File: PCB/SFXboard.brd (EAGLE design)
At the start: 34 x 31.7 mm, 17 parts, among them J1 AVR_SPI_PRG_62X3_LOCK, J2 TERMBLOCK4POS, J3 POWER_JACKPTH, Q1 16MHz, Q2 BSS138, Q3 BSS138, Q4 BSS138, U1 ATMEGA16U2-AU, X1 USBSMD

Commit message: Begin working on better power filtering, misc enhancements
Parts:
- added C5: 22uF, resistor:C0805
- added SJ1: (no value), jumper:SJ
- J1: value AVR_SPI_PRG_62X3_LOCK -> AVR_SPI_PRG_6PTH; device SparkFun-Connectors:2X3_LOCK -> SparkFun-Connectors:2X3
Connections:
- new net N$17: SJ1.1, U1.13
- net GND: now also C5.2, SJ1.2
- net N$16: now also C5.1
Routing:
- net N$16: track 26.4 -> 27.4 mm
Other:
- board text added: "Rev 2012-10-14.1"
- board text removed: "Rev 2012-09-16.1"
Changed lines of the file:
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@@
 <layer number="19" name="Unrouted" color="6" fill="1" visible="yes" active="yes"/>
 <layer number="20" name="Dimension" color="15" fill="1" visible="yes" active="yes"/>
-<layer number="21" name="tPlace" color="7" fill="1" visible="no" active="yes"/>
-<layer number="22" name="bPlace" color="7" fill="1" visible="no" active="yes"/>
-<layer number="23" name="tOrigins" color="15" fill="1" visible="no" active="yes"/>
-<layer number="24" name="bOrigins" color="15" fill="1" visible="no" active="yes"/>
-<layer number="25" name="tNames" color="7" fill="1" visible="no" active="yes"/>
-<layer number="26" name="bNames" color="7" fill="1" visible="no" active="yes"/>
-<layer number="27" name="tValues" color="7" fill="1" visible="no" active="yes"/>
-<layer number="28" name="bValues" color="7" fill="1" visible="no" active="yes"/>
+<layer number="21" name="tPlace" color="7" fill="1" visible="yes" active="yes"/>
+<layer number="22" name="bPlace" color="7" fill="1" visible="yes" active="yes"/>
+<layer number="23" name="tOrigins" color="15" fill="1" visible="yes" active="yes"/>
+<layer number="24" name="bOrigins" color="15" fill="1" visible="yes" active="yes"/>
+<layer number="25" name="tNames" color="7" fill="1" visible="yes" active="yes"/>
+<layer number="26" name="bNames" color="7" fill="1" visible="yes" active="yes"/>
+<layer number="27" name="tValues" color="7" fill="1" visible="yes" active="yes"/>
+<layer number="28" name="bValues" color="7" fill="1" visible="yes" active="yes"/>
 <layer number="29" name="tStop" color="7" fill="3" visible="no" active="yes"/>
 <layer number="30" name="bStop" color="7" fill="6" visible="no" active="yes"/>
@@
 <wire x1="0" y1="31.74" x2="0" y2="0" width="0" layer="20"/>
 <text x="2.54" y="15.24" size="1.778" layer="21" rot="R90">SFXmachine</text>
-<text x="12.319" y="13.589" size="1.016" layer="21">Rev 2012-09-16.1</text>
+<text x="12.319" y="13.589" size="1.016" layer="21">Rev 2012-10-14.1</text>
 <text x="12.446" y="12.319" size="1.016" layer="21">supersat@cs.uw.edu</text>
+<rectangle x1="13.97" y1="2.54" x2="16.51" y2="5.08" layer="16"/>
 </plain>
 <attributes>
@@
 <attribute name="VALUE" x="17.018" y="26.035" size="0.4064" layer="27"/>
 </element>
-<element name="J1" library="SparkFun-Connectors" package="2X3_LOCK" value="AVR_SPI_PRG_62X3_LOCK" x="31.75" y="11.43" smashed="yes" rot="R90"/>
+<element name="J1" library="SparkFun-Connectors" package="2X3" value="AVR_SPI_PRG_6PTH" x="31.75" y="11.43" smashed="yes" rot="R90"/>
 <element name="J2" library="sfxboard" package="TERMBLOCK4P" value="TERMBLOCK4POS" x="22.86" y="3.81"/>
 <element name="J3" library="SparkFun-Connectors" package="POWER_JACK_PTH" value="POWER_JACKPTH" x="5.08" y="0"/>
 <element name="U$2" library="SparkFun-Aesthetics" package="OSHW-LOGO-S" value="OSHW-LOGOS" x="19.05" y="16.51"/>
+<element name="C5" library="resistor" package="C0805" value="22uF" x="10.922" y="4.953" rot="MR90"/>
+<element name="SJ1" library="jumper" package="SJ" value="" x="2.54" y="-5.08"/>
 </elements>
 <signals>
@@
 <via x="15.367" y="13.843" extent="1-16" drill="0.6"/>
 <via x="19.05" y="13.97" extent="1-16" drill="0.6"/>
+<contactref element="C5" pad="2"/>
+<contactref element="SJ1" pad="2"/>
+<wire x1="5.08" y1="7.7" x2="3.302" y2="-5.08" width="0" layer="19" extent="1-1"/>
 </signal>
 <signal name="N$2">
@@
 <via x="9.525" y="20.955" extent="1-16" drill="0.6"/>
 <wire x1="9.525" y1="20.955" x2="30.48" y2="20.955" width="0.254" layer="16"/>
-<wire x1="32.004" y1="13.97" x2="30.48" y2="15.24" width="0.254" layer="16"/>
+<wire x1="31.75" y1="13.97" x2="30.48" y2="15.24" width="0.254" layer="16"/>
 <wire x1="30.48" y1="15.24" x2="30.48" y2="20.955" width="0.254" layer="16"/>
 </signal>
@@
 <contactref element="J1" pad="4"/>
 <contactref element="U1" pad="16"/>
-<wire x1="29.464" y1="13.97" x2="29.464" y2="14.224" width="0.254" layer="16"/>
+<wire x1="29.21" y1="13.97" x2="29.464" y2="14.224" width="0.254" layer="16"/>
 <wire x1="29.464" y1="14.224" x2="27.94" y2="15.24" width="0.254" layer="16"/>
 <wire x1="27.94" y1="15.24" x2="27.94" y2="20.32" width="0.254" layer="16"/>
@@
 <contactref element="J3" pad="PWR"/>
 <contactref element="J2" pad="1"/>
-<wire x1="15.24" y1="3.81" x2="1.905" y2="3.81" width="0.8128" layer="16"/>
-<wire x1="1.905" y1="3.81" x2="1.905" y2="13.7" width="0.8128" layer="16"/>
-<wire x1="1.905" y1="13.7" x2="5.08" y2="13.7" width="0.8128" layer="16"/>
+<wire x1="15.24" y1="3.81" x2="1.397" y2="3.81" width="2.032" layer="16"/>
+<wire x1="1.397" y1="3.81" x2="1.397" y2="13.7" width="2.032" layer="16"/>
+<wire x1="1.397" y1="13.7" x2="5.08" y2="13.7" width="2.032" layer="16"/>
+<contactref element="C5" pad="1"/>
+<wire x1="15.24" y1="3.81" x2="10.922" y2="4.103" width="0" layer="19" extent="16-16"/>
 </signal>
 <signal name="N$14">
@@
 <wire x1="13.1826" y1="18.5674" x2="13.1826" y2="18.79" width="0.254" layer="1"/>
 </signal>
+<signal name="N$17">
+<contactref element="SJ1" pad="1"/>
+<contactref element="U1" pad="13"/>
+<wire x1="1.778" y1="-5.08" x2="4.5974" y2="21.19" width="0" layer="19" extent="1-1"/>
+</signal>
 </signals>

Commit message: Circuit improvements, but not yet complete
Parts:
- added C6: 0.1uF, resistor:C0402
- added F1: PTC0603, SparkFun-PowerIC:0603
- added FRAME1: FRAME-LETTER, SparkFun-Aesthetics:CREATIVE_COMMONS
- added R4, R5, R6: 470, resistor:R0805
- moved SJ1 28.4 mm to (7.62, 22.9), flipped to the bottom, turned to 180 degrees
- moved U$2 26.9 mm to (38.1, -2.54)
- moved R3 2.62 mm to (22.9, 16.5)
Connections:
- new net B: R6.1, U1.23
- new net G: R5.1, U1.25
- new net N$18: C4.1, C6.1, F1.2, J1.2, R3.1, U1.31, U1.32, U1.4
- new net R: R4.1, U1.21
- net BLU_PWM: now also R6.2; no longer U1.23
- net GND: now also C6.2
- net GRN_PWM: now also R5.2; no longer U1.25
- net N$2: now also F1.1; no longer C4.1, J1.2, R3.1, U1.31, U1.32, U1.4
- net RED_PWM: now also R4.2; no longer U1.21
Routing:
- net N$2: track 38.3 -> 0.00 mm, vias 2 -> 0
- net N$18: track 0.00 -> 19.5 mm
- net GRN_PWM: track 13.9 -> 0.43 mm
- net BLU_PWM: track 12.8 -> 1.02 mm
- net RED_PWM: track 10.5 -> 0.00 mm
- net N$7: track 25.0 -> 25.8 mm
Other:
- board text added: "Rev 2012-10-31.1"
- board text removed: "Rev 2012-10-14.1"

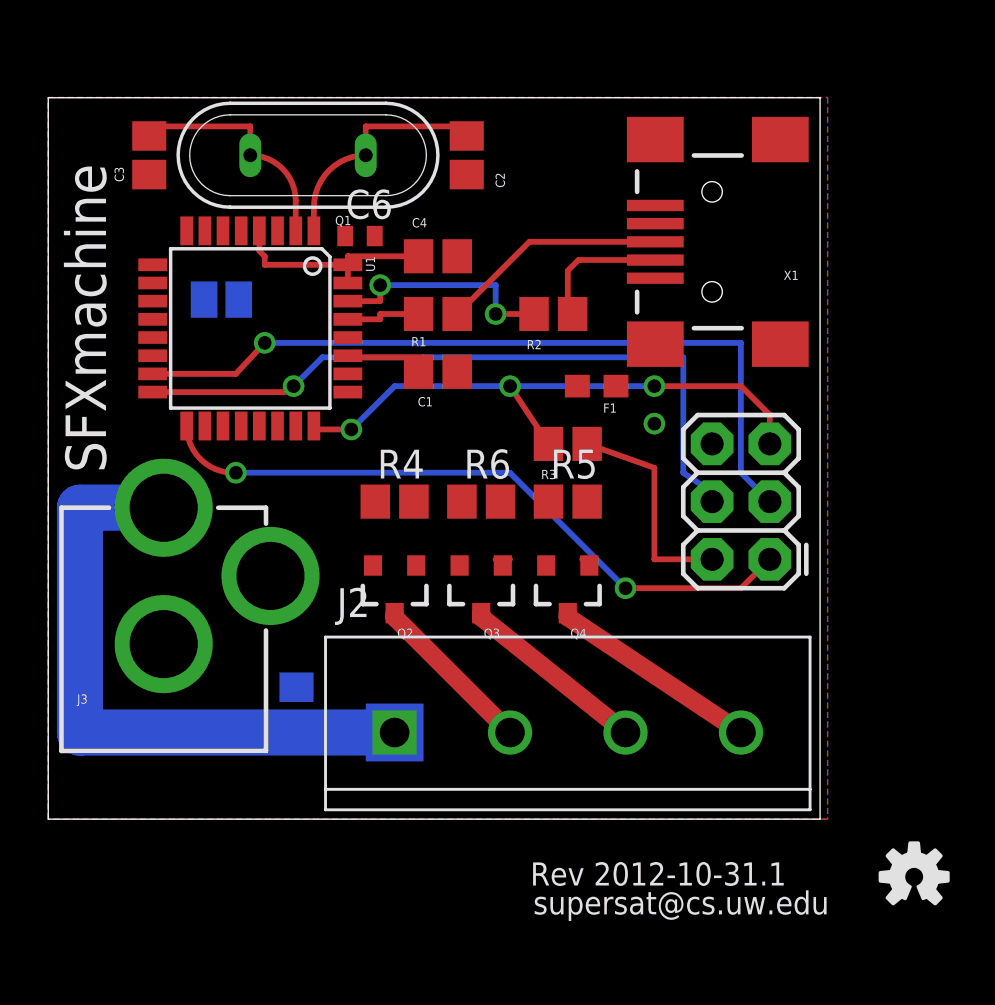
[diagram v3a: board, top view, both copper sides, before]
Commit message: New board rev with all GPIO brought out
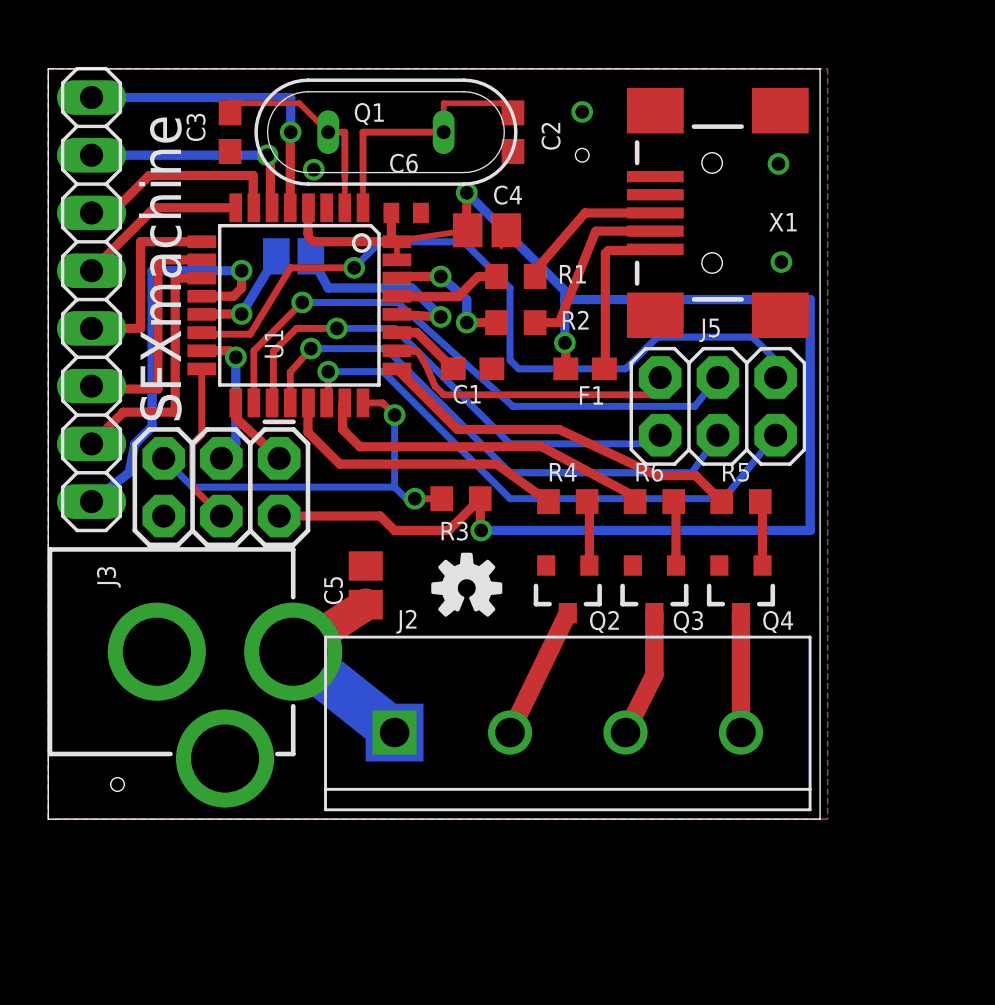
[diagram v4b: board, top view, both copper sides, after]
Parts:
- added J4: (no value), pinhead:1X08
- added J5: (no value), SparkFun-Connectors:2X03
- C1, C2, C3: device resistor:C0805 -> resistor:C0603
- R1, R2, R3, R4, R5, R6: device resistor:R0805 -> resistor:R0603
- moved U$2 23.4 mm to (18.4, 10.2)
- moved J1 22.0 mm to (10.2, 15.9), turned to 180 degrees
- moved J3 10.9 mm to (-2.92, 7.37), turned to 270 degrees
- moved Q3 7.62 mm to (26.7, 10.2)
- moved Q4 7.62 mm to (30.5, 10.2)
- moved R5 7.62 mm to (30.5, 14.0)
- moved R6 7.62 mm to (26.7, 14.0)
- moved Q2 7.62 mm to (22.9, 10.2)
- moved R4 7.62 mm to (22.9, 14.0)
- moved C5 6.14 mm to (14.0, 10.3), flipped to the top
- moved R3 5.28 mm to (18.2, 14.1)
- moved R1 3.81 mm to (20.6, 23.9)
- moved SJ1 3.70 mm to (10.8, 24.8)
- moved C3 3.70 mm to (8.00, 30.2)
- moved Q1 3.58 mm to (14.9, 30.2)
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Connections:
- new net A1: J4.1, U1.5
- new net A2: J4.2, U1.6
- new net A3: J4.3, U1.7
- new net A4: J4.4, U1.8
- new net A5: J4.5, U1.9
- new net A6: J4.6, U1.10
- new net A7: J4.7, U1.11
- new net A8: J4.8, U1.12
- new net B1: J5.1, U1.19
- new net B2: J5.2, U1.26
- new net B3: J5.3, U1.20
- new net B4: J5.4, U1.18
- new net B5: J5.5, U1.22
- new net B6: J5.6, U1.14
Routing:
- net N$18: track 19.5 -> 69.0 mm, vias 0 -> 3
- net B6: track 0.00 -> 33.9 mm, vias 0 -> 1
- net N$11: track 34.0 -> 6.33 mm
- net B4: track 0.00 -> 26.0 mm, vias 0 -> 1
- net N$12: track 29.1 -> 3.27 mm, vias 2 -> 0
- net B5: track 0.00 -> 24.7 mm, vias 0 -> 1
- net N$13: track 31.2 -> 7.17 mm, vias 1 -> 0
- net B3: track 0.00 -> 23.8 mm, vias 0 -> 1
- net B1: track 0.00 -> 22.4 mm, vias 0 -> 1
- net N$16: track 27.4 -> 9.34 mm
- net A8: track 0.00 -> 17.9 mm, vias 0 -> 1
- net G: track 0.00 -> 16.3 mm
- net B: track 0.00 -> 15.2 mm
- net B2: track 0.00 -> 13.8 mm
- net A1: track 0.00 -> 13.6 mm, vias 0 -> 1
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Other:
- board size 34 x 31.7 mm -> 34 x 33 mm
- board text added: "Rev 2012-11-23.1"
- board text removed: "Rev 2012-10-31.1"

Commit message: Final tweaks for rev2
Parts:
- moved J5 0.13 mm to (29.3, 18.2)
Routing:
- net B6: track 33.9 -> 32.9 mm
- net B2: track 13.8 -> 12.9 mm
- net N$18: track 69.0 -> 68.5 mm
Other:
- board text added: "Rev 2012-11-27.1"
- board text removed: "Rev 2012-11-23.1"
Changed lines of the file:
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@@
 <wire x1="0" y1="33.01" x2="0" y2="0" width="0" layer="20"/>
 <text x="5.842" y="17.399" size="1.778" layer="21" rot="R90">SFXmachine</text>
-<text x="32.004" y="7.366" size="1.016" layer="22" rot="MR0">Rev 2012-11-23.1</text>
+<text x="32.004" y="7.366" size="1.016" layer="22" rot="MR0">Rev 2012-11-27.1</text>
 <text x="32.004" y="5.969" size="1.016" layer="22" rot="MR0">supersat@cs.uw.edu</text>
 <rectangle x1="13.97" y1="2.54" x2="16.51" y2="5.08" layer="16"/>
@@
 <attribute name="VALUE" x="-1.27" y="33.02" size="1.27" layer="27" rot="R270"/>
 </element>
-<element name="J5" library="SparkFun-Connectors" package="2X03" value="" x="29.464" y="18.161" smashed="yes">
-<attribute name="NAME" x="28.702" y="21.209" size="0.8128" layer="25" ratio="10"/>
-<attribute name="VALUE" x="25.654" y="13.716" size="1.27" layer="27"/>
+<element name="J5" library="SparkFun-Connectors" package="2X03" value="" x="29.337" y="18.161" smashed="yes">
+<attribute name="NAME" x="28.575" y="21.209" size="0.8128" layer="25" ratio="10"/>
+<attribute name="VALUE" x="25.527" y="13.716" size="1.27" layer="27"/>
 </element>
 </elements>
@@
 <wire x1="19.939" y1="31.496" x2="20.447" y2="31.076" width="0.254" layer="1"/>
 <wire x1="13.849" y1="27.946" x2="13.849" y2="26.8986" width="0.254" layer="1"/>
-<wire x1="13.849" y1="27.946" x2="13.849" y2="30.226" width="0.3048" layer="1"/>
-<wire x1="13.849" y1="30.226" x2="17.399" y2="30.226" width="0.3048" layer="1"/>
+<wire x1="13.849" y1="27.946" x2="13.849" y2="29.458" width="0.3048" layer="1"/>
+<wire x1="13.849" y1="29.458" x2="13.843" y2="29.464" width="0.3048" layer="1"/>
+<wire x1="13.843" y1="29.464" x2="13.843" y2="29.718" width="0.3048" layer="1"/>
+<wire x1="13.843" y1="29.718" x2="14.351" y2="30.226" width="0.3048" layer="1"/>
+<wire x1="14.351" y1="30.226" x2="17.399" y2="30.226" width="0.3048" layer="1"/>
 </signal>
 <signal name="N$9">
@@
 <wire x1="15.3416" y1="19.806" x2="18.0026" y2="17.145" width="0.4064" layer="1"/>
 <wire x1="18.0026" y1="17.145" x2="22.479" y2="17.145" width="0.4064" layer="1"/>
-<wire x1="26.797" y1="15.113" x2="28.487" y2="15.113" width="0.4064" layer="1"/>
+<wire x1="26.035" y1="15.113" x2="28.487" y2="15.113" width="0.4064" layer="1"/>
 <wire x1="28.487" y1="15.113" x2="29.63" y2="13.97" width="0.4064" layer="1"/>
-<wire x1="26.797" y1="15.113" x2="22.479" y2="17.145" width="0.4064" layer="1"/>
+<wire x1="26.035" y1="15.113" x2="22.479" y2="17.145" width="0.4064" layer="1"/>
 </signal>
 <signal name="B">
@@
 <wire x1="15.24" y1="12.7" x2="14.605" y2="13.335" width="0.4064" layer="1"/>
 <wire x1="14.605" y1="13.335" x2="10.16" y2="13.335" width="0.4064" layer="1"/>
-<wire x1="15.0876" y1="25.4" x2="18.454" y2="25.908" width="0.254" layer="1"/>
+<wire x1="15.0876" y1="25.4" x2="18.454" y2="25.908" width="0.4064" layer="1"/>
 <wire x1="19.011" y1="14.097" x2="19.011" y2="12.7" width="0.4064" layer="1"/>
 <wire x1="19.011" y1="12.7" x2="19.05" y2="12.7" width="0.4064" layer="1"/>
 <via x="19.05" y="12.7" extent="1-16" drill="0.6"/>
-<wire x1="19.05" y1="12.7" x2="33.528" y2="12.7" width="0.4064" layer="16"/>
-<wire x1="33.528" y1="12.7" x2="33.528" y2="22.86" width="0.4064" layer="16"/>
-<wire x1="33.528" y1="22.86" x2="22.733" y2="22.86" width="0.4064" layer="16"/>
+<wire x1="19.05" y1="12.7" x2="33.274" y2="12.7" width="0.4064" layer="16"/>
+<wire x1="33.274" y1="12.7" x2="33.274" y2="22.86" width="0.4064" layer="16"/>
+<wire x1="33.274" y1="22.86" x2="22.733" y2="22.86" width="0.4064" layer="16"/>
 </signal>
 <signal name="N$2">
@@
 <wire x1="16.637" y1="19.939" x2="17.018" y2="19.05" width="0.3048" layer="1"/>
 <wire x1="17.018" y1="19.05" x2="17.399" y2="18.669" width="0.3048" layer="1"/>
-<wire x1="17.399" y1="18.669" x2="26.543" y2="18.669" width="0.3048" layer="1"/>
-<wire x1="26.543" y1="18.669" x2="27.305" y2="19.431" width="0.3048" layer="1"/>
-<wire x1="27.305" y1="19.431" x2="26.924" y2="19.431" width="0.3048" layer="1"/>
+<wire x1="17.399" y1="18.669" x2="26.035" y2="18.669" width="0.3048" layer="1"/>
+<wire x1="26.035" y1="18.669" x2="26.797" y2="19.431" width="0.3048" layer="1"/>
 </signal>
 <signal name="B4">
@@
 <wire x1="15.367" y1="22.733" x2="20.447" y2="18.161" width="0.3048" layer="16"/>
 <wire x1="20.447" y1="18.161" x2="28.448" y2="18.161" width="0.3048" layer="16"/>
-<wire x1="28.448" y1="18.161" x2="29.464" y2="19.431" width="0.3048" layer="16"/>
+<wire x1="28.448" y1="18.161" x2="29.337" y2="19.431" width="0.3048" layer="16"/>
 </signal>
 <signal name="B6">
@@
 <via x="13.462" y="24.257" extent="1-16" drill="0.6"/>
 <wire x1="20.32" y1="20.193" x2="20.701" y2="19.812" width="0.3048" layer="16"/>
-<wire x1="20.701" y1="19.812" x2="25.4" y2="19.812" width="0.3048" layer="16"/>
-<wire x1="25.4" y1="19.812" x2="26.797" y2="21.209" width="0.3048" layer="16"/>
-<wire x1="26.797" y1="21.209" x2="30.988" y2="21.209" width="0.3048" layer="16"/>
-<wire x1="30.988" y1="21.209" x2="32.512" y2="19.685" width="0.3048" layer="16"/>
-<wire x1="32.512" y1="19.685" x2="32.004" y2="19.431" width="0.3048" layer="16"/>
+<wire x1="20.701" y1="19.812" x2="24.892" y2="19.812" width="0.3048" layer="16"/>
+<wire x1="24.892" y1="19.812" x2="26.289" y2="21.209" width="0.3048" layer="16"/>
+<wire x1="26.289" y1="21.209" x2="30.353" y2="21.209" width="0.3048" layer="16"/>
+<wire x1="30.353" y1="21.209" x2="31.877" y2="19.685" width="0.3048" layer="16"/>
+<wire x1="31.877" y1="19.685" x2="31.877" y2="19.431" width="0.3048" layer="16"/>
 <wire x1="13.462" y1="24.257" x2="14.605" y2="25.4" width="0.3048" layer="16"/>
 <wire x1="14.605" y1="25.4" x2="18.288" y2="25.4" width="0.3048" layer="16"/>
@@
 <wire x1="12.7" y1="21.59" x2="15.24" y2="21.59" width="0.3048" layer="16"/>
 <wire x1="15.24" y1="21.59" x2="20.32" y2="16.51" width="0.3048" layer="16"/>
-<wire x1="20.32" y1="16.51" x2="27.051" y2="16.51" width="0.3048" layer="16"/>
-<wire x1="27.051" y1="16.51" x2="26.924" y2="16.891" width="0.3048" layer="16"/>
 <wire x1="12.7" y1="21.59" x2="10.922" y2="21.59" width="0.3048" layer="1"/>
 <wire x1="10.922" y1="21.59" x2="9.906" y2="20.574" width="0.3048" layer="1"/>
 <wire x1="9.906" y1="20.574" x2="9.906" y2="18.3704" width="0.3048" layer="1"/>
 <wire x1="9.906" y1="18.3704" x2="9.849" y2="18.3134" width="0.3048" layer="1"/>
+<wire x1="20.32" y1="16.51" x2="26.416" y2="16.51" width="0.3048" layer="16"/>
+<wire x1="26.416" y1="16.51" x2="26.797" y2="16.891" width="0.3048" layer="16"/>
 </signal>
 <signal name="B3">
@@
 <wire x1="14.859" y1="20.701" x2="20.32" y2="15.24" width="0.3048" layer="16"/>
 <wire x1="20.32" y1="15.24" x2="28.321" y2="15.24" width="0.3048" layer="16"/>
-<wire x1="28.321" y1="15.24" x2="29.464" y2="16.891" width="0.3048" layer="16"/>
+<wire x1="28.321" y1="15.24" x2="29.337" y2="16.891" width="0.3048" layer="16"/>
 </signal>
 <signal name="B5">
@@
 <wire x1="14.732" y1="19.685" x2="20.32" y2="14.097" width="0.3048" layer="16"/>
 <wire x1="20.32" y1="14.097" x2="29.718" y2="14.097" width="0.3048" layer="16"/>
-<wire x1="29.718" y1="14.097" x2="32.004" y2="16.891" width="0.3048" layer="16"/>
+<wire x1="29.718" y1="14.097" x2="31.877" y2="16.891" width="0.3048" layer="16"/>
 </signal>
 </signals>
